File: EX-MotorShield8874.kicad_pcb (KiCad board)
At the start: 4 copper layers, 68.6 x 53.3 mm, 96 parts, among them J1 Power, J11 I2C, J12 OLED, J13 MC 1,5/ 2-G-3,5, J14 STEMMA QT, J15 MC 1,5/ 2-G-3,5, J2 Digital/PWM, J3 Analog, J4 Digital/PWM, J51 Barrel_Jack_MountingPin, Q11 AO3400A, Q12 AO3400A, Q51 AOD4185, Q52 LP2301LT1G, SW101 RESET, U12 74HC32, U13 74HC04, U14 74HC08, U15 DRV8874PWPR, U16 DRV8874PWPR, U51 TPS5430DDA

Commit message: Update BOM to include all parts.
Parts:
- removed C14, C15, C18, C20, C21, C24, C55, C56, C57: 100nF, Capacitor_SMD:C_0402_1005Metric
- removed C16, C22: 10uF, Capacitor_SMD:C_0805_2012Metric
- removed C17, C19, C23, C25: 22nF, Capacitor_SMD:C_0402_1005Metric
- removed C58, C59: 100uF, Capacitor_SMD:CP_Elec_6.3x7.7
- removed D53: EMERALD, LED_SMD:LED_0603_1608Metric
- removed JP11: PWMA, Jumper:SolderJumper-3_P1.3mm_Bridged12_RoundedPad1.0x1.5mm
- removed JP12: BRKA, Jumper:SolderJumper-3_P1.3mm_Bridged12_RoundedPad1.0x1.5mm
- removed JP13: PWMB, Jumper:SolderJumper-3_P1.3mm_Bridged12_RoundedPad1.0x1.5mm
- removed JP14: BRKB, Jumper:SolderJumper-3_P1.3mm_Bridged12_RoundedPad1.0x1.5mm
- removed JP15: DIRB, Jumper:SolderJumper-3_P1.3mm_Bridged12_RoundedPad1.0x1.5mm
- removed JP16: DIRA, Jumper:SolderJumper-3_P1.3mm_Bridged12_RoundedPad1.0x1.5mm
- removed JP17: FLTA, Jumper:SolderJumper-3_P1.3mm_Bridged12_RoundedPad1.0x1.5mm
- removed JP18: FLTB, Jumper:SolderJumper-3_P1.3mm_Bridged12_RoundedPad1.0x1.5mm
- removed JP19: SENB, Jumper:SolderJumper-3_P1.3mm_Bridged12_RoundedPad1.0x1.5mm
- removed JP20: SENA, Jumper:SolderJumper-3_P1.3mm_Bridged12_RoundedPad1.0x1.5mm
- removed JP23: PMODE, Jumper:SolderJumper-3_P1.3mm_Bridged12_RoundedPad1.0x1.5mm
- removed JP24: ph/in2a, Jumper:SolderJumper-3_P1.3mm_Bridged12_RoundedPad1.0x1.5mm
- removed JP25: nSleepb, Jumper:SolderJumper-3_P1.3mm_Bridged12_RoundedPad1.0x1.5mm
- removed JP26: ph/in2b, Jumper:SolderJumper-3_P1.3mm_Bridged12_RoundedPad1.0x1.5mm
- removed JP27: nSleepa, Jumper:SolderJumper-3_P1.3mm_Bridged12_RoundedPad1.0x1.5mm
- removed JP51: IO OVRID, Jumper:SolderJumper-3_P1.3mm_Bridged12_RoundedPad1.0x1.5mm
- removed JP52: 3or5, Jumper:SolderJumper-3_P1.3mm_Bridged12_RoundedPad1.0x1.5mm
- removed JP53: REG EN, Jumper:SolderJumper-2_P1.3mm_Bridged_RoundedPad1.0x1.5mm
- removed JP54: BYP, Jumper:SolderJumper-2_P1.3mm_Open_RoundedPad1.0x1.5mm
- removed JP55: Vdrive->VCOM, Jumper:SolderJumper-2_P1.3mm_Open_RoundedPad1.0x1.5mm
- removed JP56: REG OUT, Jumper:SolderJumper-2_P1.3mm_Bridged_RoundedPad1.0x1.5mm
- removed JP57: B/P A, Jumper:SolderJumper-3_P1.3mm_Bridged12_RoundedPad1.0x1.5mm
- removed JP58: INA, Jumper:SolderJumper-3_P1.3mm_Bridged12_RoundedPad1.0x1.5mm
- removed JP59: INB, Jumper:SolderJumper-3_P1.3mm_Bridged12_RoundedPad1.0x1.5mm
- removed JP60: B/P B, Jumper:SolderJumper-3_P1.3mm_Bridged12_RoundedPad1.0x1.5mm
- removed Q11, Q12: AO3400A, Package_TO_SOT_SMD:SOT-23
- removed Q52: LP2301LT1G, Package_TO_SOT_SMD:SOT-23
- removed R11, R15, R16, R17, R18, R20, R23, R55: 47K, Resistor_SMD:R_0402_1005Metric
- removed R19, R22: 1K43, Resistor_SMD:R_0402_1005Metric
- removed R21, R24: 732R, Resistor_SMD:R_0402_1005Metric
- removed R51: 470K, Resistor_SMD:R_0402_1005Metric
- removed U12: 74HC32, Package_SO:TSSOP-14_4.4x5mm_P0.65mm
- removed U13: 74HC04, Package_SO:TSSOP-14_4.4x5mm_P0.65mm
- removed U14: 74HC08, Package_SO:TSSOP-14_4.4x5mm_P0.65mm
- removed U15, U16: DRV8874PWPR, Package_SO:HTSSOP-16-1EP_4.4x5mm_P0.65mm_EP3.4x5mm_Mask2.46x2.31mm_ThermalVias
- added C102: 20pF, Capacitor_SMD:C_0402_1005Metric, F.Cu at (197.8, 75.3)
- added C103: 20pF, Capacitor_SMD:C_0402_1005Metric, F.Cu at (197.8, 77.2)
- added C104: 20pF, Capacitor_SMD:C_0402_1005Metric, F.Cu at (197.8, 79.2)
- added C105: 20pF, Capacitor_SMD:C_0402_1005Metric, F.Cu at (197.8, 81.2)
- added C301: 100uF, Capacitor_SMD:CP_Elec_6.3x7.7, F.Cu at (214.3, 73.8)
- added C302: 10uF, Capacitor_SMD:C_0805_2012Metric, F.Cu at (220.2, 83.3)
- added C303: 100nF, Capacitor_SMD:C_0402_1005Metric, F.Cu at (207.6, 70.7)
- added C304: 100nF, Capacitor_SMD:C_0402_1005Metric, F.Cu at (207.6, 72.7)
- added C305: 22nF, Capacitor_SMD:C_0402_1005Metric, F.Cu at (207.6, 74.6)
- added C306: 100nF, Capacitor_SMD:C_0402_1005Metric, F.Cu at (207.6, 76.6)
- added C307: 22nF, Capacitor_SMD:C_0402_1005Metric, F.Cu at (207.6, 78.6)
- added C401: 100uF, Capacitor_SMD:CP_Elec_6.3x7.7, F.Cu at (214.3, 56.6)
- added C402: 10uF, Capacitor_SMD:C_0805_2012Metric, F.Cu at (220.2, 66.2)
- added C403: 100nF, Capacitor_SMD:C_0402_1005Metric, F.Cu at (207.6, 53.6)
- added C404: 100nF, Capacitor_SMD:C_0402_1005Metric, F.Cu at (207.6, 55.5)
- added C405: 22nF, Capacitor_SMD:C_0402_1005Metric, F.Cu at (207.6, 57.5)
- added C406: 100nF, Capacitor_SMD:C_0402_1005Metric, F.Cu at (207.6, 59.5)
- added C407: 22nF, Capacitor_SMD:C_0402_1005Metric, F.Cu at (207.6, 61.4)
- added D203: EMERALD, LED_SMD:LED_0603_1608Metric, F.Cu at (181.9, 86.7)
- added J105: JTAG, Connector_PinHeader_2.54mm:PinHeader_2x05_P2.54mm_Vertical, F.Cu at (199.3, 54.9)
- added J109: USB_B_Micro, Connector_USB:USB_Micro-B_Molex-105017-0001, F.Cu at (184.8, 77.3)
- added R202: 47K, Resistor_SMD:R_0402_1005Metric, F.Cu at (181.3, 89.0)
- added R301: 47K, Resistor_SMD:R_0402_1005Metric, F.Cu at (219.4, 78.9)
- added R302: 1K24, Resistor_SMD:R_0402_1005Metric, F.Cu at (219.4, 80.8)
- added R401: 47K, Resistor_SMD:R_0402_1005Metric, F.Cu at (219.4, 61.7)
- added R402: 1K24, Resistor_SMD:R_0402_1005Metric, F.Cu at (219.4, 63.7)
- added U101: ESP32-S2-MINI-2, PCM_Espressif:ESP32-S2-MINI-1, F.Cu at (188.4, 65.7)
- added U301: DRV8874PWPR, Package_SO:HTSSOP-16-1EP_4.4x5mm_P0.65mm_EP3.4x5mm_Mask2.46x2.31mm_ThermalVias, F.Cu at (213.5, 81.2)
- added U401: DRV8874PWPR, Package_SO:HTSSOP-16-1EP_4.4x5mm_P0.65mm_EP3.4x5mm_Mask2.46x2.31mm_ThermalVias, F.Cu at (213.5, 64.0)
- added Y101: 40Mhz, Crystal:Crystal_SMD_5032-4Pin_5.0x3.2mm, F.Cu at (200.3, 69.8)
- R203: renamed from R53; value 49K9 -> 17K4
- SW101: value RESET -> FLASH
- moved SW101 37.2 mm to (193.0, 78.9)
- renumbered C13 to C101, C53 to C201, C54 to C202, C51 to C203, C52 to C204, D54 to D101, D55 to D102, D52 to D201, D51 to D202, J13 to J101, J11 to J102, J14 to J103, J2 to J104, J1 to J106, J15 to J107, J12 to J108, J3 to J110, J4 to J111, J51 to J201, L51 to L201, Q51 to Q201, R13 to R101, R14 to R102, R52 to R201, R54 to R204, U51 to U201
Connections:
- C202 pad 1: /Power/REGOUT -> +3V3
- J102 pad 1: VBUS -> +3V3
- J102 pad 2: VBUS -> +3V3
- J106 pad 2: IOREF -> +3V3
- J106 pad 3: /reset -> unconnected-(J106-Pin_3-Pad3)
- J106 pad 5: +5V -> unconnected-(J106-Pin_5-Pad5)
- J106 pad 8: VCOM -> unconnected-(J106-Pin_8-Pad8)
- J108 pad 2: VBUS -> +3V3
- L201 pad 2: /Power/REGOUT -> +3V3
- R203 pad 2: /Power/REGOUT -> +3V3
- SW101 pad 1: /reset -> /BOOT_MODE
- U201 pad 5: /Power/en -> Vdrive
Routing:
- net (no net): track 0.00 -> 894.8 mm, vias 0 -> 50
- net /sen_b: track 59.3 -> 0.00 mm, vias 4 -> 0
- net /fault_n_b: track 59.2 -> 0.00 mm, vias 4 -> 0
- net +3V3: track 99.6 -> 156.9 mm, vias 2 -> 14
- net /sen_a: track 56.3 -> 0.00 mm, vias 4 -> 0
- net /fault_n_a: track 48.7 -> 0.00 mm, vias 4 -> 0
- net /pwm_b: track 41.5 -> 0.00 mm, vias 3 -> 0
- net /direction_b: track 38.3 -> 0.00 mm, vias 2 -> 0
- net /pmode: track 37.2 -> 0.00 mm, vias 3 -> 0
- net /brake_a: track 36.2 -> 0.00 mm
- net /brake_b_n: track 36.1 -> 0.00 mm, vias 2 -> 0
- net /pwm_a: track 35.7 -> 0.00 mm, vias 2 -> 0
- net /direction_a: track 35.4 -> 0.00 mm, vias 3 -> 0
- net /brake_b: track 33.6 -> 0.00 mm, vias 2 -> 0
- net unconnected-(J106-Pin_3-Pad3): track 0.00 -> 33.4 mm, vias 0 -> 1
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- added copper zone on F.Cu, net +3V3
- added copper zone on In2.Cu, net +3V3
- removed copper zone on F.Cu, net /Power/REGOUT
- removed copper zone on In2.Cu, net VBUS

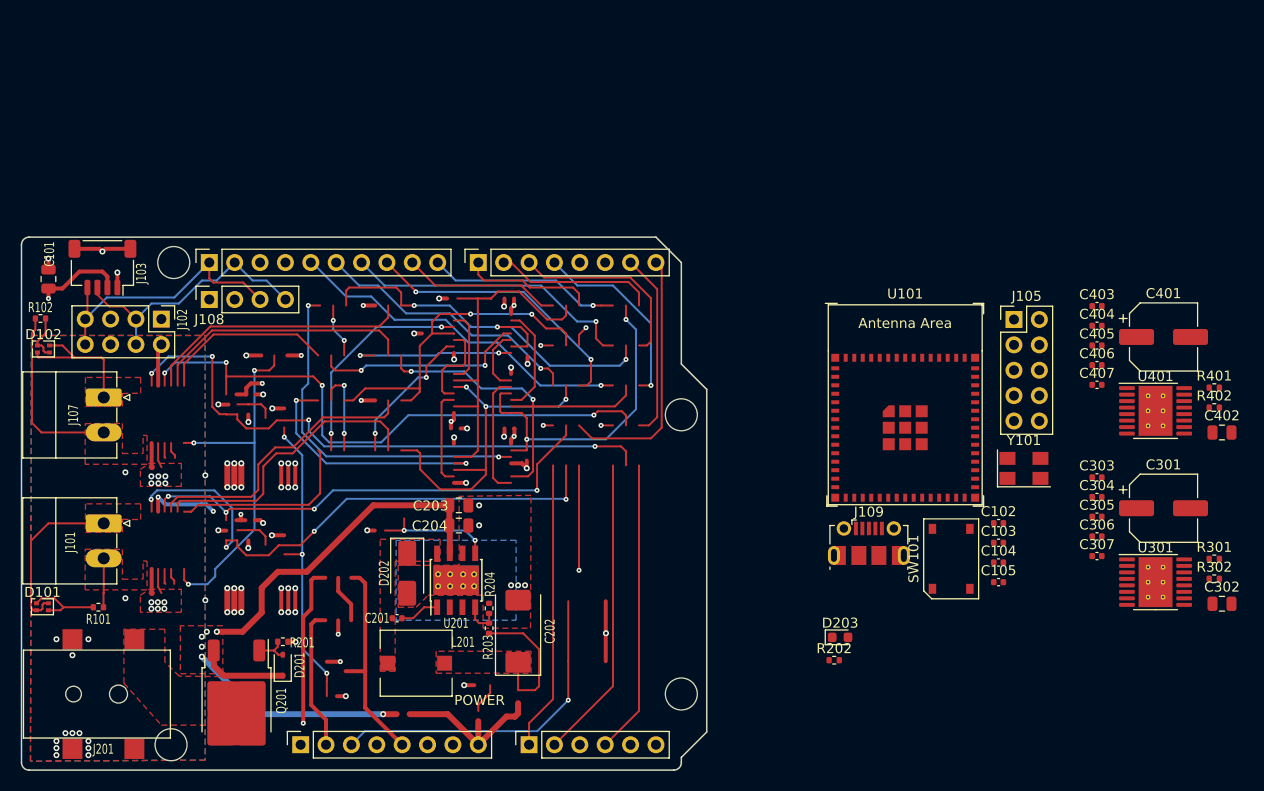
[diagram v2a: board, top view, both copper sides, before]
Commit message: Initial attempt to route the board.
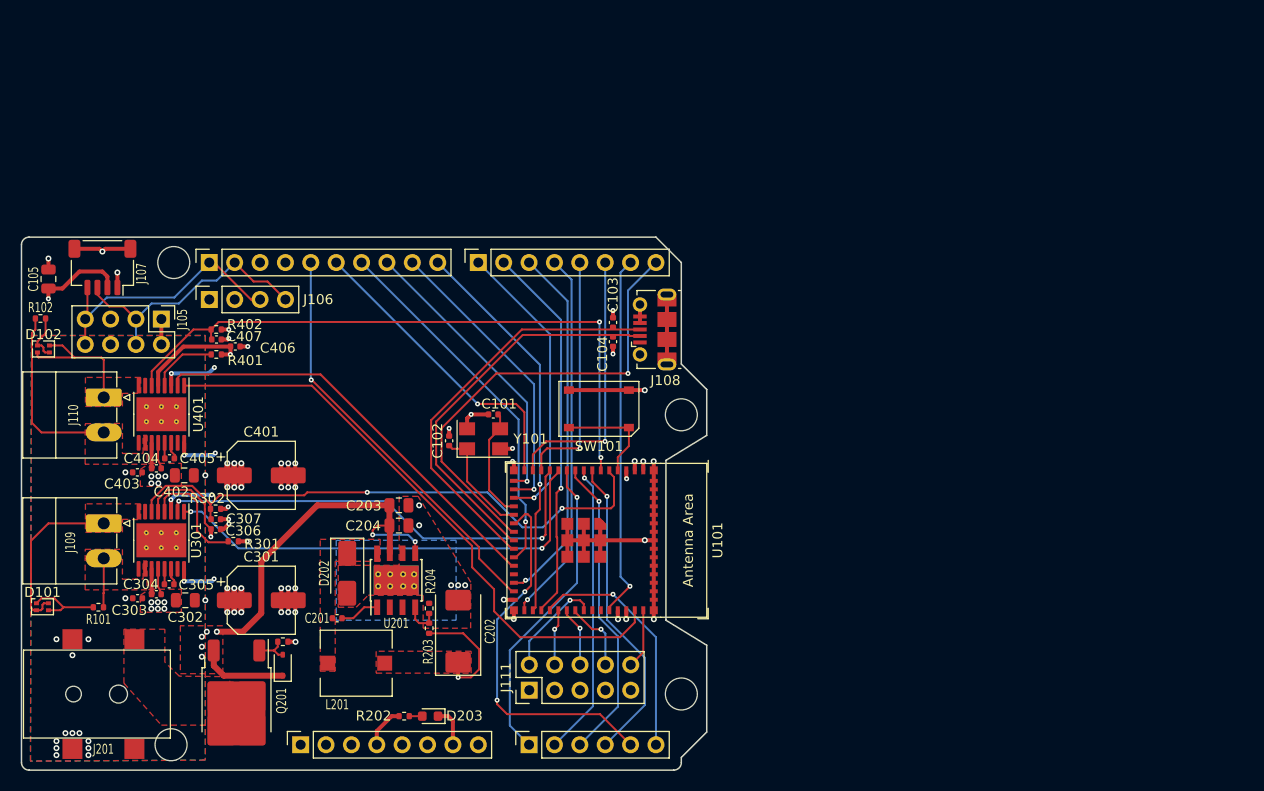
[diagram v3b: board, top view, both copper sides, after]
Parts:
- moved C402 103.9 mm to (116.3, 70.5)
- moved C302 103.8 mm to (116.4, 83.0)
- moved R402 100.2 mm to (119.5, 55.9)
- moved R302 100.2 mm to (119.4, 73.8)
- moved R401 99.9 mm to (119.5, 58.4), turned to 180 degrees
- moved U301 99.6 mm to (114.0, 77.0), turned to -90 degrees
- moved U401 99.5 mm to (114.0, 64.4), turned to -90 degrees
- moved R301 98.2 mm to (121.2, 77.1), turned to 180 degrees
- moved C403 97.5 mm to (111.6, 70.2), turned to 180 degrees
- moved C303 96.8 mm to (111.6, 82.8), turned to 180 degrees
- moved C404 95.2 mm to (113.5, 69.8)
- moved C304 94.6 mm to (113.5, 82.4)
- moved C405 93.5 mm to (114.8, 68.8), turned to 180 degrees
- moved C305 93.1 mm to (114.8, 81.4), turned to 180 degrees
- moved C401 91.4 mm to (124.0, 70.5)
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- renumbered C104 to C101, C105 to C102, C102 to C103, C103 to C104, C101 to C105, J106 to J101, J110 to J102, J104 to J103, J111 to J104, J102 to J105, J108 to J106, J103 to J107, J109 to J108, J101 to J109, J107 to J110, J105 to J111
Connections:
- J111 pad 3: Net-(J105-Pin_3) -> GND
- J111 pad 5: Net-(J105-Pin_3) -> GND
- J111 pad 9: Net-(J105-Pin_3) -> GND
- U101 pad 10: /alt_sen_b -> /def_sen_a
- U101 pad 7: /def_sen_a -> /alt_sen_b
- U101 pad 8: /alt_sen_a -> /def_sen_b
- U101 pad 9: /def_sen_b -> /alt_sen_a
- U301 pad 10: /trk1l -> /trk1r
- U301 pad 8: /trk1r -> /trk1l
- U401 pad 10: /trk2l -> /trk2r
- U401 pad 8: /trk2r -> /trk2l
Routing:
- net (no net): track 894.8 -> 0.00 mm, vias 50 -> 0
- net +3V3: track 156.9 -> 71.5 mm
- net /Out2-Vpropi: track 0.00 -> 64.2 mm, vias 0 -> 2
- net /Out2-IN1: track 0.00 -> 59.9 mm
- net /Out1-Vpropi: track 0.00 -> 56.9 mm, vias 0 -> 2
- net /Out1-IN2: track 0.00 -> 46.1 mm, vias 0 -> 2
- net /Out1-IN1: track 0.00 -> 45.8 mm, vias 0 -> 2
- net GND: track 51.4 -> 96.8 mm, vias 61 -> 59
- net /Out2-IN2: track 0.00 -> 42.5 mm
- net /USB_D+: track 0.00 -> 41.1 mm
- net /USB_D-: track 0.00 -> 39.3 mm
- net unconnected-(J101-Pin_3-Pad3): track 33.4 -> 0.00 mm, vias 1 -> 0
- net Vdrive: track 96.7 -> 66.5 mm, vias 32 -> 30
- net /alt_brake_b: track 16.1 -> 38.0 mm, vias 0 -> 1
- net unconnected-(J101-Pin_5-Pad5): track 21.3 -> 0.00 mm
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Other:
- outline, holes or cut-outs redrawn
- board text removed: "POWER"

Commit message: Stand alone, purpose build command station doodle.
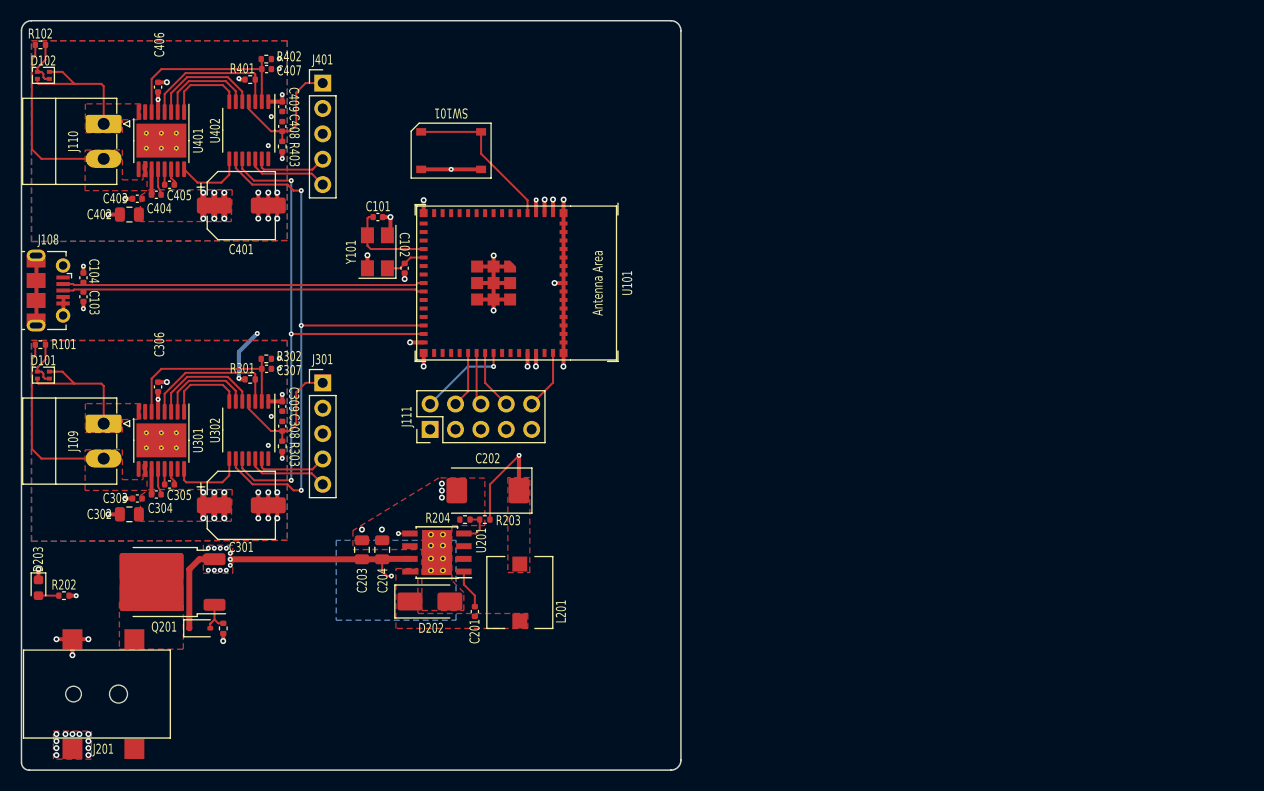
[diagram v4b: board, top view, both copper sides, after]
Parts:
- removed C105: 22uF, Capacitor_SMD:C_0805_2012Metric
- removed J101: Power, Connector_PinSocket_2.54mm:PinSocket_1x08_P2.54mm_Vertical
- removed J102: Analog, Connector_PinSocket_2.54mm:PinSocket_1x06_P2.54mm_Vertical
- removed J103: Digital/PWM, Connector_PinSocket_2.54mm:PinSocket_1x10_P2.54mm_Vertical
- removed J104: Digital/PWM, Connector_PinSocket_2.54mm:PinSocket_1x08_P2.54mm_Vertical
- removed J105: I2C, Connector_PinHeader_2.54mm:PinHeader_2x04_P2.54mm_Vertical
- removed J106: OLED, Connector_PinSocket_2.54mm:PinSocket_1x04_P2.54mm_Vertical
- removed J107: STEMMA QT, Connector_JST:JST_SH_SM04B-SRSS-TB_1x04-1MP_P1.00mm_Horizontal
- removed MH1, MH2, MH3, MH4: MountingHole_3.2mm, DCC-EX-Footprints:MountingHole_3.2mm
- added C308: 100nF, Capacitor_SMD:C_0402_1005Metric, F.Cu at (126.1, 65.6)
- added C309: 100nF, Capacitor_SMD:C_0402_1005Metric, F.Cu at (126.1, 63.6)
- added C408: 100nF, Capacitor_SMD:C_0402_1005Metric, F.Cu at (126.1, 35.6)
- added C409: 100nF, Capacitor_SMD:C_0402_1005Metric, F.Cu at (126.1, 33.6)
- added J301: ICSP, Connector_PinHeader_2.54mm:PinHeader_1x05_P2.54mm_Vertical, F.Cu at (130.2, 61.2)
- added J401: ICSP, Connector_PinHeader_2.54mm:PinHeader_1x05_P2.54mm_Vertical, F.Cu at (130.2, 31.2)
- added R303: 10K, Resistor_SMD:R_0402_1005Metric, F.Cu at (126.1, 67.6)
- added R403: 10K, Resistor_SMD:R_0402_1005Metric, F.Cu at (126.1, 37.6)
- added U302: PIC16F15224-I/ST, Package_SO:TSSOP-14_4.4x5mm_P0.65mm, F.Cu at (122.8, 66.0)
- added U402: PIC16F15224-I/ST, Package_SO:TSSOP-14_4.4x5mm_P0.65mm, F.Cu at (122.8, 36.0)
- U101: value ESP32-S2-MINI-2 -> ESP32-S2-MINI-2U
- moved J108 60.8 mm to (102.7, 52.0), turned to -90 degrees
- moved C104 53.4 mm to (106.2, 50.7), turned to 90 degrees
- moved C103 53.1 mm to (106.2, 52.6), turned to -90 degrees
- moved D203 41.3 mm to (101.7, 81.8), turned to -90 degrees
- moved R202 36.1 mm to (104.2, 82.5), turned to 0 degrees
- moved SW101 29.8 mm to (143.0, 38.0), turned to -90 degrees
- moved J111 27.9 mm to (140.9, 65.9)
- moved R401 27.7 mm to (122.9, 30.9), turned to 0 degrees
- moved C407 27.5 mm to (124.5, 29.8)
- moved R402 27.5 mm to (124.5, 28.8)
- moved C403 27.4 mm to (111.6, 42.8)
- moved C404 27.4 mm to (113.5, 42.4)
- moved C405 27.4 mm to (114.8, 41.4)
- moved D102 27.4 mm to (102.2, 30.5)
- moved J110 27.4 mm to (108.2, 35.3)
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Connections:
- net /Out1-Fault renamed /Output 1/nFault
- net /Out2-Fault renamed /Output 2/nFault
- C307 pad 1: /Out1-Vpropi -> /Output 1/VPROPI
- C407 pad 1: /Out2-Vpropi -> /Output 2/VPROPI
- R302 pad 1: /Out1-Vpropi -> /Output 1/VPROPI
- R402 pad 1: /Out2-Vpropi -> /Output 2/VPROPI
- U101 pad 10: /def_sen_a -> unconnected-(U101-GPIO6/ADC1_CH5-Pad10)
- U101 pad 11: /Out1-IN1 -> unconnected-(U101-GPIO7/ADC1_CH6-Pad11)
- U101 pad 12: /Out1-IN2 -> unconnected-(U101-GPIO8/ADC1_CH7-Pad12)
- U101 pad 13: /def_pwm_a -> unconnected-(U101-GPIO9/ADC1_CH8-Pad13)
- U101 pad 14: /alt_pwm_a -> unconnected-(U101-GPIO10/ADC1_CH9-Pad14)
- U101 pad 15: /def_direction_a -> unconnected-(U101-GPIO11/ADC2_CH0-Pad15)
- U101 pad 16: /alt_direction_a -> unconnected-(U101-GPIO12/ADC2_CH1-Pad16)
- U101 pad 17: /def_brake_a -> unconnected-(U101-GPIO13/ADC2_CH2-Pad17)
- U101 pad 18: /alt_brake_a -> unconnected-(U101-GPIO14/ADC2_CH3-Pad18)
- U101 pad 21: /def_fault_n_a -> unconnected-(U101-ADC2_CH7/DAC_2/GPIO17-Pad21)
- U101 pad 22: /alt_fault_n_a -> unconnected-(U101-ADC2_CH6/DAC_1/GPIO18-Pad22)
- U101 pad 25: /def_pwm_b -> unconnected-(U101-GPIO21-Pad25)
- U101 pad 26: /Out2-IN2 -> unconnected-(U101-SPI_CS1/GPIO26-Pad26)
- U101 pad 28: /alt_pwm_b -> /SDA
- U101 pad 29: /def_direction_b -> /SCL
- U101 pad 31: /alt_direction_b -> unconnected-(U101-GPIO35-Pad31)
- U101 pad 32: /def_brake_b -> unconnected-(U101-GPIO36-Pad32)
- U101 pad 33: /alt_brake_b -> unconnected-(U101-GPIO37-Pad33)
- U101 pad 34: /def_fault_n_b -> unconnected-(U101-GPIO38-Pad34)
- U101 pad 41: /alt_fault_n_b -> unconnected-(U101-GPIO45-Pad41)
- U101 pad 44: /Out2-IN1 -> unconnected-(U101-GPIO46-Pad44)
- U101 pad 5: /Out1-Vpropi -> unconnected-(U101-GPIO1/ADC1_CH0-Pad5)
- U101 pad 6: /Out2-Vpropi -> unconnected-(U101-GPIO2/ADC1_CH1-Pad6)
- U101 pad 7: /alt_sen_b -> unconnected-(U101-GPIO3/ADC1_CH2-Pad7)
- U101 pad 8: /def_sen_b -> unconnected-(U101-GPIO4/ADC1_CH3-Pad8)
- U101 pad 9: /alt_sen_a -> unconnected-(U101-GPIO5/ADC1_CH4-Pad9)
- U301 pad 1: /Out1-IN1 -> /Output 1/EN/IN1
- U301 pad 16: +3V3 -> /Output 1/PMODE
- U301 pad 2: /Out1-IN2 -> /Output 1/PH/IN2
- U301 pad 3: +3V3 -> /Output 1/nSleep
- U301 pad 6: /Out1-Vpropi -> /Output 1/VPROPI
- U401 pad 1: /Out2-IN1 -> /Output 2/EN/IN1
- U401 pad 16: +3V3 -> /Output 2/PMODE
- U401 pad 2: /Out2-IN2 -> /Output 2/PH/IN2
- U401 pad 3: +3V3 -> /Output 2/nSleep
- U401 pad 6: /Out2-Vpropi -> /Output 2/VPROPI
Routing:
- net /Out2-Vpropi: track 64.2 -> 0.00 mm, vias 2 -> 0
- net /Out2-IN1: track 59.9 -> 0.00 mm
- net /SDA: track 0.00 -> 59.0 mm, vias 0 -> 3
- net /Out1-Vpropi: track 56.9 -> 0.00 mm, vias 2 -> 0
- net /SCL: track 0.00 -> 56.0 mm, vias 0 -> 3
- net /alt_fault_n_a: track 46.7 -> 0.00 mm, vias 1 -> 0
- net /Out1-IN2: track 46.1 -> 0.00 mm, vias 2 -> 0
- net /Out1-IN1: track 45.8 -> 0.00 mm, vias 2 -> 0
- net /Out2-IN2: track 42.5 -> 0.00 mm
- net +3V3: track 71.5 -> 30.0 mm, vias 14 -> 12
- net /def_direction_b: track 41.5 -> 0.00 mm, vias 1 -> 0
- net /def_brake_b: track 39.3 -> 0.00 mm, vias 1 -> 0
- net /alt_brake_b: track 38.0 -> 0.00 mm, vias 1 -> 0
- net /alt_direction_b: track 37.5 -> 0.00 mm, vias 1 -> 0
- net /def_fault_n_a: track 37.4 -> 0.00 mm, vias 2 -> 0
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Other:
- board size 68.6 x 53.3 mm -> 66 x 75 mm
